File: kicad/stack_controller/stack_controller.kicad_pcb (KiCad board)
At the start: 2 copper layers, 24 parts

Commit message: Possibly final design of stack controller
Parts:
- added U26: ~, Package_DIP:DIP-20_W7.62mm, F.Cu at (40.2, 146.0)
- added U27: ~, Package_DIP:DIP-14_W7.62mm, F.Cu at (40.2, 126.6)
- added U28: ~, Package_DIP:DIP-14_W7.62mm, F.Cu at (51.1, 126.6)
- added U29: ~, Package_DIP:DIP-20_W7.62mm, F.Cu at (51.1, 146.0)
- added U30: ~, Package_DIP:DIP-20_W7.62mm, F.Cu at (62.0, 146.0)
- added U31: ~, Package_DIP:DIP-14_W7.62mm, F.Cu at (62.0, 126.6)
- added U32: ~, Connector_PinHeader_2.54mm:PinHeader_1x08_P2.54mm_Vertical, F.Cu at (73.5, 146.2)
- added U33: ~, Connector_PinHeader_2.54mm:PinHeader_1x16_P2.54mm_Vertical, F.Cu at (36.3, 126.8)
- U12, U8: footprint Package_DIP:DIP-48_W15.24mm -> Package_DIP:DIP-20_W7.62mm
- U9: footprint Package_DIP:DIP-14_W7.62mm -> Package_DIP:DIP-20_W7.62mm
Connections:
- U1 pad 16: Net-(U1-V+) -> Net-(U1-B0)
- U1 pad 7: Net-(U1-B0) -> Net-(U1-C_IN)
- U1 pad 8: Net-(U1-B0) -> Net-(U1-C_IN)
- U10 pad 14: Net-(U1-B0) -> Net-(U1-C_IN)
- U10 pad 28: Net-(U1-V+) -> Net-(U1-B0)
- U11 pad 14: Net-(U1-B0) -> Net-(U1-C_IN)
- U11 pad 22: Net-(U11-OE#) -> Net-(U10-OE#)
- U11 pad 27: Net-(U11-WE#) -> Net-(U10-WE#)
- U11 pad 28: Net-(U1-V+) -> Net-(U1-B0)
- U12 pad 1: Net-(U1-B0) -> Net-(U1-C_IN)
- U12 pad 10: (no net) -> Net-(U1-C_IN)
- U12 pad 11: unconnected-(U12-QA6-Pad11) -> Net-(U12-CLK)
- U12 pad 12: unconnected-(U12-QA7-Pad12) -> Net-(U12-Q7)
- U12 pad 13: Net-(U12-DA0) -> Net-(U12-Q6)
- U12 pad 14: Net-(U1-B1) -> Net-(U12-Q5)
- U12 pad 15: (no net) -> Net-(U12-Q4)
- U12 pad 16: Net-(U12-DA1) -> Net-(U12-Q3)
- U12 pad 17: Net-(U12-QB3) -> Net-(U12-Q2)
- U12 pad 18: (no net) -> Net-(U12-Q1)
- U12 pad 19: Net-(U12-DA2) -> Net-(U12-Q0)
- U12 pad 2: Net-(U12-DB1) -> Net-(U12-D0)
- U12 pad 20: Net-(U12-DA3) -> Net-(U1-B0)
- U12 pad 3: Net-(U12-DB3) -> Net-(U12-D1)
- U12 pad 4: Net-(U1-B0) -> Net-(U12-D2)
- U12 pad 5: Net-(U12-DB5) -> Net-(U12-D3)
- U12 pad 6: Net-(U12-DB6) -> Net-(U12-D4)
- U12 pad 7: Net-(U1-V+) -> Net-(U12-D5)
- U12 pad 8: unconnected-(U12-QA4-Pad8) -> Net-(U12-D6)
- U12 pad 9: unconnected-(U12-QA5-Pad9) -> Net-(U12-D7)
- U13 pad 1: Net-(U12-QB6) -> Net-(U11-CE#)
- U13 pad 10: unconnected-(U13-4A-Pad10) -> Net-(U13-O4)
- U13 pad 11: unconnected-(U13-3Q-Pad11) -> Net-(U13-I4)
- U13 pad 13: unconnected-(U13-3A-Pad13) -> Net-(U1-C_IN)
- U13 pad 14: Net-(U1-V+) -> Net-(U1-B0)
- U13 pad 2: Net-(U12-CLK_B) -> Net-(U10-CE#)
- U13 pad 3: unconnected-(U13-1Q-Pad3) -> Net-(U13-I1)
- U13 pad 4: Net-(U12-QB3) -> Net-(U10-OE#)
- U13 pad 5: Net-(U12-CLK_A) -> Net-(U13-I2)
- U13 pad 6: Net-(U13-2Q) -> Net-(U10-WE#)
- U13 pad 7: Net-(U1-B0) -> Net-(U1-C_IN)
- U13 pad 8: unconnected-(U13-4Q-Pad8) -> Net-(U13-03)
- U13 pad 9: unconnected-(U13-4B-Pad9) -> Net-(U13-I3)
- U14 pad 16: Net-(U1-V+) -> Net-(U1-B0)
- U14 pad 7: Net-(U1-V+) -> Net-(U1-C_IN)
- U14 pad 8: Net-(U1-B0) -> Net-(U1-C_IN)
- U15 pad 16: Net-(U1-V+) -> Net-(U1-B0)
- U15 pad 8: Net-(U1-B0) -> Net-(U1-C_IN)
- U16 pad 11: Net-(U1-V+) -> Net-(U1-B0)
- U16 pad 12: Net-(U16-A3) -> Net-(U12-D3)
- U16 pad 14: Net-(U16-A2) -> Net-(U12-D2)
- U16 pad 15: Net-(U1-V+) -> Net-(U1-B0)
- U16 pad 16: Net-(U1-V+) -> Net-(U1-B0)
- U16 pad 2: Net-(U1-V+) -> Net-(U1-B0)
- U16 pad 3: Net-(U16-A1) -> Net-(U12-D1)
- U16 pad 5: Net-(U16-A0) -> Net-(U12-D0)
- U16 pad 6: Net-(U1-V+) -> Net-(U1-B0)
- U16 pad 8: Net-(U1-B0) -> Net-(U1-C_IN)
- U17 pad 11: Net-(U1-V+) -> Net-(U1-B0)
- U17 pad 12: Net-(U17-A3) -> Net-(U12-D7)
- U17 pad 14: Net-(U17-A2) -> Net-(U12-D6)
- U17 pad 15: Net-(U1-V+) -> Net-(U1-B0)
- U17 pad 16: Net-(U1-V+) -> Net-(U1-B0)
- U17 pad 2: Net-(U1-V+) -> Net-(U1-B0)
- U17 pad 3: Net-(U17-A1) -> Net-(U12-D5)
- U17 pad 5: Net-(U17-A0) -> Net-(U12-D4)
- U17 pad 6: Net-(U1-V+) -> Net-(U1-B0)
- U17 pad 8: Net-(U1-B0) -> Net-(U1-C_IN)
- U18 pad 1: Net-(U1-V+) -> Net-(U1-B0)
- U18 pad 10: Net-(U1-B0) -> Net-(U1-C_IN)
- U18 pad 12: Net-(U15-B0) -> Net-(U15-B3)
- U18 pad 13: Net-(U10-D4) -> Net-(U15-B2)
- U18 pad 14: Net-(U10-D5) -> Net-(U15-B1)
- U18 pad 15: Net-(U15-B1) -> Net-(U15-B0)
- U18 pad 16: Net-(U15-B2) -> Net-(U14-B3)
- U18 pad 17: Net-(U10-D6) -> Net-(U14-B2)
- U18 pad 18: Net-(U10-D7) -> Net-(U14-B1)
- U18 pad 19: Net-(U15-B3) -> Net-(U14-B0)
- U18 pad 2: Net-(U14-B0) -> Net-(U18-D0)
- U18 pad 20: Net-(U1-V+) -> Net-(U1-B0)
- U18 pad 3: Net-(U10-D0) -> Net-(U18-D1)
- U18 pad 4: Net-(U10-D1) -> Net-(U18-D2)
- U18 pad 5: Net-(U14-B1) -> Net-(U18-D3)
- U18 pad 6: Net-(U14-B2) -> Net-(U18-D4)
- U18 pad 7: Net-(U10-D2) -> Net-(U18-D5)
- U18 pad 8: Net-(U10-D3) -> Net-(U18-D6)
- U18 pad 9: Net-(U14-B3) -> Net-(U18-D7)
- U19 pad 1: unconnected-(U19-I0-Pad1) -> Net-(U13-03)
- U19 pad 10: Net-(U10-OE#) -> Net-(U19-4A)
- U19 pad 11: unconnected-(U19-I4-Pad11) -> Net-(U13-I4)
- U19 pad 12: Net-(U10-WE#) -> Net-(U19-2B)
- U19 pad 13: Net-(U19-I5) -> Net-(U13-03)
- U19 pad 14: Net-(U1-V+) -> Net-(U1-B0)
- U19 pad 2: Net-(U11-CE#) -> Net-(U19-1B)
- U19 pad 3: unconnected-(U19-I1-Pad3) -> Net-(U13-I1)
- U19 pad 4: Net-(U11-OE#) -> Net-(U19-1B)
- U19 pad 5: Net-(U19-I2) -> Net-(U19-2B)
- U19 pad 6: Net-(U11-WE#) -> Net-(U13-I3)
- U19 pad 7: Net-(U1-B0) -> Net-(U1-C_IN)
- U19 pad 8: Net-(U10-CE#) -> Net-(U19-4Q)
- U19 pad 9: unconnected-(U19-I3-Pad9) -> Net-(U12-CLK)
- U2 pad 16: Net-(U1-V+) -> Net-(U1-B0)
- U2 pad 8: Net-(U1-B0) -> Net-(U1-C_IN)
- U20 pad 10: Net-(U14-Σ3) -> Net-(U14-Σ2)
- U20 pad 11: Net-(U14-A3) -> Net-(U14-A2)
- U20 pad 12: Net-(U10-A2) -> Net-(U10-A3)
- U20 pad 13: Net-(U14-Σ2) -> Net-(U14-Σ3)
- U20 pad 14: Net-(U14-A2) -> Net-(U14-A3)
- U20 pad 15: Net-(U1-B0) -> Net-(U1-C_IN)
- U20 pad 16: Net-(U1-V+) -> Net-(U1-B0)
- U20 pad 8: Net-(U1-B0) -> Net-(U1-C_IN)
- U20 pad 9: Net-(U10-A3) -> Net-(U10-A2)
- U21 pad 10: Net-(U15-Σ3) -> Net-(U15-Σ2)
- U21 pad 11: Net-(U15-A3) -> Net-(U15-A2)
- U21 pad 12: Net-(U10-A6) -> Net-(U10-A7)
- U21 pad 13: Net-(U15-Σ2) -> Net-(U15-Σ3)
- U21 pad 14: Net-(U15-A2) -> Net-(U15-A3)
- U21 pad 15: Net-(U1-B0) -> Net-(U1-C_IN)
- U21 pad 16: Net-(U1-V+) -> Net-(U1-B0)
- U21 pad 8: Net-(U1-B0) -> Net-(U1-C_IN)
- U21 pad 9: Net-(U10-A7) -> Net-(U10-A6)
- U22 pad 10: Net-(U16-Σ3) -> Net-(U16-Σ2)
- U22 pad 11: Net-(U16-A3) -> Net-(U12-D2)
- U22 pad 12: Net-(U10-A10) -> Net-(U10-A11)
- U22 pad 13: Net-(U16-Σ2) -> Net-(U16-Σ3)
- U22 pad 14: Net-(U16-A2) -> Net-(U12-D3)
- U22 pad 15: Net-(U1-B0) -> Net-(U1-C_IN)
- U22 pad 16: Net-(U1-V+) -> Net-(U1-B0)
- U22 pad 2: Net-(U16-A0) -> Net-(U12-D0)
- U22 pad 5: Net-(U16-A1) -> Net-(U12-D1)
- U22 pad 8: Net-(U1-B0) -> Net-(U1-C_IN)
- U22 pad 9: Net-(U10-A11) -> Net-(U10-A10)
- U23 pad 10: Net-(U17-Σ3) -> Net-(U17-Σ2)
- U23 pad 11: Net-(U17-A3) -> Net-(U12-D6)
- U23 pad 12: Net-(U10-A14) -> Net-(U11-CE#)
- U23 pad 13: Net-(U17-Σ2) -> Net-(U17-Σ3)
- U23 pad 14: Net-(U17-A2) -> Net-(U12-D7)
- U23 pad 15: Net-(U1-B0) -> Net-(U1-C_IN)
- U23 pad 16: Net-(U1-V+) -> Net-(U1-B0)
- U23 pad 2: Net-(U17-A0) -> Net-(U12-D4)
- U23 pad 5: Net-(U17-A1) -> Net-(U12-D5)
- U23 pad 8: Net-(U1-B0) -> Net-(U1-C_IN)
- U23 pad 9: Net-(U23-Q3) -> Net-(U10-A14)
- U24 pad 1: Net-(U23-Q3) -> Net-(U24-1A)
- U24 pad 10: unconnected-(U24-Q2-Pad10) -> Net-(U24-4A)
- U24 pad 11: unconnected-(U24-Q3-Pad11) -> Net-(U24-3Q)
- U24 pad 12: unconnected-(U24-3A-Pad12) -> Net-(U24-2A)
- U24 pad 13: unconnected-(U24-3B-Pad13) -> Net-(U24-3A)
- U24 pad 14: Net-(U1-V+) -> Net-(U1-B0)
- U24 pad 2: unconnected-(U24-0B-Pad2) -> Net-(U1-B1)
- U24 pad 3: Net-(U19-I2) -> Net-(U24-1Q)
- U24 pad 4: Net-(U19-I5) -> Net-(U24-2A)
- U24 pad 5: Net-(U24-1A) -> Net-(U24-2B)
- U24 pad 6: unconnected-(U24-1B-Pad6) -> Net-(U13-I2)
- U24 pad 7: Net-(U1-B0) -> Net-(U1-C_IN)
- U24 pad 8: unconnected-(U24-2A-Pad8) -> Net-(U24-4Q)
- U24 pad 9: unconnected-(U24-2B-Pad9) -> Net-(U24-2A)
- U25 pad 1: Net-(U23-Q3) -> Net-(U25-0A)
- U25 pad 10: unconnected-(U25-O4-Pad10) -> Net-(U24-3A)
- U25 pad 11: unconnected-(U25-I4-Pad11) -> Net-(U25-Q3)
- U25 pad 12: unconnected-(U25-O5-Pad12) -> Net-(U13-I3)
- U25 pad 13: unconnected-(U25-I5-Pad13) -> Net-(U19-4Q)
- U25 pad 14: Net-(U1-V+) -> Net-(U1-B0)
- U25 pad 2: Net-(U24-1A) -> Net-(U1-B1)
- U25 pad 3: unconnected-(U25-I1-Pad3) -> Net-(U19-1B)
- U25 pad 5: unconnected-(U25-I2-Pad5) -> Net-(U1-C_IN)
- U25 pad 6: unconnected-(U25-O2-Pad6) -> Net-(U1-C_IN)
- U25 pad 7: Net-(U1-B0) -> Net-(U1-C_IN)
- U25 pad 8: unconnected-(U25-03-Pad8) -> Net-(U25-2A)
- U25 pad 9: unconnected-(U25-I3-Pad9) -> Net-(U25-2B)
- U3 pad 12: Net-(U3-A3) -> Net-(U12-Q3)
- U3 pad 14: Net-(U3-A2) -> Net-(U12-Q2)
- U3 pad 16: Net-(U1-V+) -> Net-(U1-B0)
- U3 pad 3: Net-(U3-A1) -> Net-(U12-Q1)
- U3 pad 5: Net-(U3-A0) -> Net-(U12-Q0)
- U3 pad 8: Net-(U1-B0) -> Net-(U1-C_IN)
- U4 pad 12: Net-(U4-A3) -> Net-(U12-Q7)
- U4 pad 14: Net-(U4-A2) -> Net-(U12-Q6)
- U4 pad 16: Net-(U1-V+) -> Net-(U1-B0)
- U4 pad 3: Net-(U4-A1) -> Net-(U12-Q5)
- U4 pad 5: Net-(U4-A0) -> Net-(U12-Q4)
- U4 pad 8: Net-(U1-B0) -> Net-(U1-C_IN)
- U6 pad 1: Net-(U1-V+) -> Net-(U1-C_IN)
- U6 pad 10: Net-(U1-B0) -> Net-(U1-C_IN)
- U6 pad 11: Net-(U13-2Q) -> Net-(U19-4A)
- U6 pad 12: Net-(U15-A0) -> Net-(U15-A3)
- U6 pad 13: Net-(U2-Σ0) -> Net-(U15-A2)
- U6 pad 14: Net-(U2-Σ1) -> Net-(U15-A1)
- U6 pad 15: Net-(U15-A1) -> Net-(U15-A0)
- U6 pad 16: Net-(U15-A2) -> Net-(U14-A3)
- U6 pad 17: Net-(U2-Σ2) -> Net-(U14-A2)
- U6 pad 18: Net-(U2-Σ3) -> Net-(U14-A1)
- U6 pad 19: Net-(U15-A3) -> Net-(U14-A0)
- U6 pad 2: Net-(U14-A0) -> Net-(U1-Σ0)
- U6 pad 20: Net-(U1-V+) -> Net-(U1-B0)
- U6 pad 3: Net-(U1-Σ0) -> Net-(U1-Σ1)
- U6 pad 4: Net-(U1-Σ1) -> Net-(U1-Σ2)
- U6 pad 5: Net-(U14-A1) -> Net-(U1-Σ3)
- U6 pad 6: Net-(U14-A2) -> Net-(U2-Σ0)
- U6 pad 7: Net-(U1-Σ2) -> Net-(U2-Σ1)
- U6 pad 8: Net-(U1-Σ3) -> Net-(U2-Σ2)
- U6 pad 9: Net-(U14-A3) -> Net-(U2-Σ3)
- U7 pad 1: Net-(U1-V+) -> Net-(U1-C_IN)
- U7 pad 10: Net-(U1-B0) -> Net-(U1-C_IN)
- U7 pad 11: Net-(U13-2Q) -> Net-(U19-4A)
- U7 pad 12: Net-(U17-A0) -> Net-(U12-D7)
- U7 pad 13: Net-(U4-Σ0) -> Net-(U12-D6)
- U7 pad 14: Net-(U4-Σ1) -> Net-(U12-D5)
- U7 pad 15: Net-(U17-A1) -> Net-(U12-D4)
- U7 pad 16: Net-(U17-A2) -> Net-(U12-D3)
- U7 pad 17: Net-(U4-Σ2) -> Net-(U12-D2)
- U7 pad 18: Net-(U4-Σ3) -> Net-(U12-D1)
- U7 pad 19: Net-(U17-A3) -> Net-(U12-D0)
- U7 pad 2: Net-(U16-A0) -> Net-(U3-Σ0)
- U7 pad 20: Net-(U1-V+) -> Net-(U1-B0)
- U7 pad 3: Net-(U3-Σ0) -> Net-(U3-Σ1)
- U7 pad 4: Net-(U3-Σ1) -> Net-(U3-Σ2)
- U7 pad 5: Net-(U16-A1) -> Net-(U3-Σ3)
- U7 pad 6: Net-(U16-A2) -> Net-(U4-Σ0)
- U7 pad 7: Net-(U3-Σ2) -> Net-(U4-Σ1)
- U7 pad 8: Net-(U3-Σ3) -> Net-(U4-Σ2)
- U7 pad 9: Net-(U16-A3) -> Net-(U4-Σ3)
- U8 pad 1: Net-(U1-B0) -> Net-(U1-C_IN)
- U8 pad 10: (no net) -> Net-(U1-C_IN)
- U8 pad 11: Net-(U2-A2) -> Net-(U12-CLK)
- U8 pad 13: Net-(U3-A0) -> Net-(U2-A2)
- U8 pad 14: Net-(U3-A1) -> Net-(U2-A1)
- U8 pad 15: (no net) -> Net-(U2-A0)
- U8 pad 16: Net-(U3-A2) -> Net-(U1-A3)
- U8 pad 17: Net-(U3-A3) -> Net-(U1-A2)
- U8 pad 18: (no net) -> Net-(U1-A1)
- U8 pad 19: Net-(U4-A0) -> Net-(U1-A0)
- U8 pad 2: Net-(U1-A0) -> Net-(U14-A0)
- U8 pad 20: Net-(U4-A1) -> Net-(U1-B0)
- U8 pad 3: Net-(U1-A1) -> Net-(U14-A1)
- U8 pad 4: Net-(U1-B0) -> Net-(U14-A2)
- U8 pad 5: Net-(U1-A2) -> Net-(U14-A3)
- U8 pad 6: Net-(U1-A3) -> Net-(U15-A0)
- U8 pad 7: Net-(U1-V+) -> Net-(U15-A1)
- U8 pad 8: Net-(U2-A0) -> Net-(U15-A2)
- U8 pad 9: Net-(U2-A1) -> Net-(U15-A3)
- U9 pad 1: Net-(U12-DB0) -> Net-(U1-C_IN)
- U9 pad 10: unconnected-(U9-Q2-Pad10) -> Net-(U1-C_IN)
- U9 pad 11: unconnected-(U9-Q3-Pad11) -> Net-(U24-2A)
- U9 pad 12: unconnected-(U9-3A-Pad12) -> Net-(U26-D6)
- U9 pad 13: unconnected-(U9-3B-Pad13) -> Net-(U26-D5)
- U9 pad 14: Net-(U1-V+) -> Net-(U24-4A)
- U9 pad 2: Net-(U5-READ_0) -> Net-(U26-Q0)
- U9 pad 3: Net-(U12-DB2) -> Net-(U24-3A)
- U9 pad 4: Net-(U12-DB4) -> Net-(U26-Q2)
- U9 pad 5: Net-(U5-READ_0) -> Net-(U19-2B)
- U9 pad 6: Net-(U5-READ_1) -> Net-(U25-2B)
- U9 pad 7: Net-(U1-B0) -> Net-(U26-Q4)
- U9 pad 8: unconnected-(U9-2A-Pad8) -> Net-(U25-2A)
- U9 pad 9: unconnected-(U9-2B-Pad9) -> Net-(U26-Q5)

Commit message: kicad stuff and timing
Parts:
- added U34: ~, custom_footprint_library:jumper, F.Cu at (256.5, 212.9)
- added U35: ~, custom_footprint_library:jumper, F.Cu at (256.5, 220.5)
- added U36: ~, custom_footprint_library:jumper, F.Cu at (256.4, 228.3)
- added U37: ~, custom_footprint_library:jumper, F.Cu at (256.5, 236.3)
- added U38: ~, custom_footprint_library:jumper, F.Cu at (256.5, 244.3)
- added U39: ~, custom_footprint_library:jumper, F.Cu at (300.7, 213.3)
- added U40: ~, custom_footprint_library:jumper, F.Cu at (300.7, 221.3)
- added U41: ~, custom_footprint_library:jumper, F.Cu at (300.7, 229.2)
- added U42: ~, custom_footprint_library:jumper, F.Cu at (300.7, 236.8)
- added U43: ~, custom_footprint_library:jumper, F.Cu at (300.7, 244.6)
- added U44: ~, custom_footprint_library:jumper, F.Cu at (300.6, 252.5)
- added U45: ~, custom_footprint_library:jumper, F.Cu at (256.8, 257.3)
- added U46: ~, custom_footprint_library:jumper, F.Cu at (256.8, 265.3)
- added U5: ~, Connector_PinHeader_2.54mm:PinHeader_1x22_P2.54mm_Vertical, F.Cu at (151.5, 259.5)
- moved U29 284.4 mm to (331.9, 190.9), turned to -90 degrees
- moved U33 269.8 mm to (305.5, 143.7), turned to 90 degrees
- moved U13 263.9 mm to (342.0, 210.3)
- moved U32 258.9 mm to (329.3, 185.9), turned to -90 degrees
- moved U19 239.0 mm to (342.4, 179.9)
- moved U30 219.7 mm to (276.3, 194.1), turned to 90 degrees
- moved U27 213.4 mm to (216.0, 247.5), turned to -90 degrees
- moved U26 209.4 mm to (225.9, 242.8)
- moved U1 203.8 mm to (229.7, 119.1)
- moved U11 196.6 mm to (323.7, 154.8), turned to -90 degrees
- moved U31 192.0 mm to (232.7, 214.4)
- moved U16 191.7 mm to (243.1, 181.5), turned to -90 degrees
- moved U28 185.4 mm to (216.2, 210.9)
- moved U10 184.7 mm to (361.1, 154.8), turned to -90 degrees
- moved U9 181.4 mm to (185.0, 239.8)
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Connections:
- U13 pad 12: unconnected-(U13-O5-Pad12) -> Net-(U13-O5)
- U13 pad 13: Net-(U1-C_IN) -> Net-(U13-I5)
- U18 pad 1: Net-(U1-B0) -> Net-(U1-C_IN)
- U24 pad 2: Net-(U1-B1) -> Net-(U24-1B)
- U24 pad 6: Net-(U13-I2) -> Net-(U24-2Q)
- U25 pad 12: Net-(U13-I3) -> Net-(U25-3A)
- U25 pad 13: Net-(U19-4Q) -> Net-(U25-3B)
- U25 pad 2: Net-(U1-B1) -> Net-(U24-1B)
- U25 pad 3: Net-(U19-1B) -> Net-(U25-Q0)
- U26 pad 16: Net-(U19-2B) -> Net-(U26-Q3)
- U27 pad 10: Net-(U19-4A) -> Net-(U27-Q2)
- U27 pad 11: Net-(U12-CLK) -> Net-(U27-Q3)
- U27 pad 4: Net-(U20-S) -> Net-(U27-Q1)
- U28 pad 1: Net-(U19-1B) -> Net-(U25-Q0)
- U28 pad 6: Net-(U18-CLK) -> Net-(U28-2Q)
- U29 pad 1: Net-(U26-Q0) -> Net-(U13-O5)
- U29 pad 11: Net-(U27-3B) -> Net-(U29-CLK)
- U30 pad 11: Net-(U24-3Q) -> Net-(U30-CLK)
- U9 pad 5: Net-(U19-2B) -> Net-(U26-Q3)
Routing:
- net Net-(U1-C_IN): track 0.00 -> 1158.8 mm, vias 0 -> 5
- net Net-(U1-B0): track 0.00 -> 828.4 mm, vias 0 -> 8
- net Net-(U15-A0): track 0.00 -> 273.5 mm, vias 0 -> 5
- net Net-(U1-B1): track 0.00 -> 272.3 mm, vias 0 -> 4
- net Net-(U12-CLK): track 0.00 -> 255.5 mm, vias 0 -> 3
- net Net-(U14-A0): track 0.00 -> 251.6 mm, vias 0 -> 2
- net Net-(U15-A1): track 0.00 -> 224.2 mm, vias 0 -> 4
- net Net-(U14-A1): track 0.00 -> 210.6 mm, vias 0 -> 3
- net Net-(U19-4A): track 0.00 -> 206.1 mm, vias 0 -> 1
- net Net-(U18-D0): track 0.00 -> 205.9 mm, vias 0 -> 1
- net Net-(U14-A3): track 0.00 -> 202.8 mm, vias 0 -> 4
- net Net-(U18-D1): track 0.00 -> 200.0 mm
- net Net-(U18-D2): track 0.00 -> 195.7 mm, vias 0 -> 1
- net Net-(U18-D3): track 0.00 -> 190.8 mm, vias 0 -> 1
- net Net-(U14-A2): track 0.00 -> 190.1 mm, vias 0 -> 3
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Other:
- board text added: "MEMORY BUS SIMULTANEOUS WRITE ADDRESS LATCHES SIMULTANEOUS HIGH"
- board text added: "Pointer adder input latch CLK Pointer inc (0) / dec (1) select Pointer latch CLK ToS (0) / offset (1) select Offset latch CLK"
- board text added: "Read (mem output enable) Write Input latch CLK Input latch output enable Output latch CLK Output latch output enable"

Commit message: stuff
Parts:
- added U47: ~, Package_DIP:DIP-14_W7.62mm, F.Cu at (115.0, 151.1)
- U5: footprint Connector_PinHeader_2.54mm:PinHeader_1x22_P2.54mm_Vertical -> Connector_PinHeader_2.54mm:PinHeader_1x23_P2.54mm_Vertical
- moved U1 155.9 mm to (105.5, 24.8)
- moved U10 155.9 mm to (236.9, 60.5)
- moved U11 155.9 mm to (199.5, 60.5)
- moved U13 155.9 mm to (217.8, 116.1)
- moved U14 155.9 mm to (42.8, 72.0)
- moved U15 155.9 mm to (84.5, 78.3)
- moved U16 155.9 mm to (118.9, 87.2)
- moved U17 155.9 mm to (128.5, 80.8)
- moved U19 155.9 mm to (218.2, 85.6)
- moved U2 155.9 mm to (85.5, 25.3)
- moved U20 155.9 mm to (136.9, 67.5)
- moved U21 155.9 mm to (148.4, 50.5)
- moved U22 155.9 mm to (151.9, 32.6)
- moved U24 155.9 mm to (55.2, 120.2)
- moved U25 155.9 mm to (73.2, 116.1)
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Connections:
- U44 pad 1: Net-(U26-Q0) -> Net-(U44-IN)
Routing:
- net Net-(U47-1B): track 0.00 -> 118.7 mm, vias 0 -> 8
- net Net-(U26-Q0): track 186.0 -> 116.9 mm, vias 2 -> 1
- net Net-(U44-IN): track 0.00 -> 67.2 mm, vias 0 -> 1
- net Net-(U26-Q5): track 0.00 -> 62.2 mm
- net Net-(U1-C_IN): track 1158.8 -> 1210.7 mm
- net Net-(U26-Q3): track 140.7 -> 166.9 mm, vias 1 -> 2
- net Net-(U25-3A): track 98.5 -> 113.8 mm, vias 1 -> 3
- net Net-(U26-CLK): track 151.3 -> 139.0 mm, vias 2 -> 1
- net Net-(U25-0A): track 93.7 -> 82.1 mm
- net Net-(U18-D7): track 174.3 -> 162.8 mm
- net Net-(U25-2B): track 80.0 -> 68.5 mm, vias 3 -> 2
- net Net-(U25-Q3): track 60.0 -> 48.5 mm
- net Net-(U18-D5): track 181.2 -> 170.0 mm
- net Net-(U24-2A): track 125.0 -> 114.6 mm, vias 0 -> 1
- net Net-(U18-D3): track 190.8 -> 180.7 mm, vias 1 -> 0
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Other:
- board outline added: 208.5 x 156.5 mm

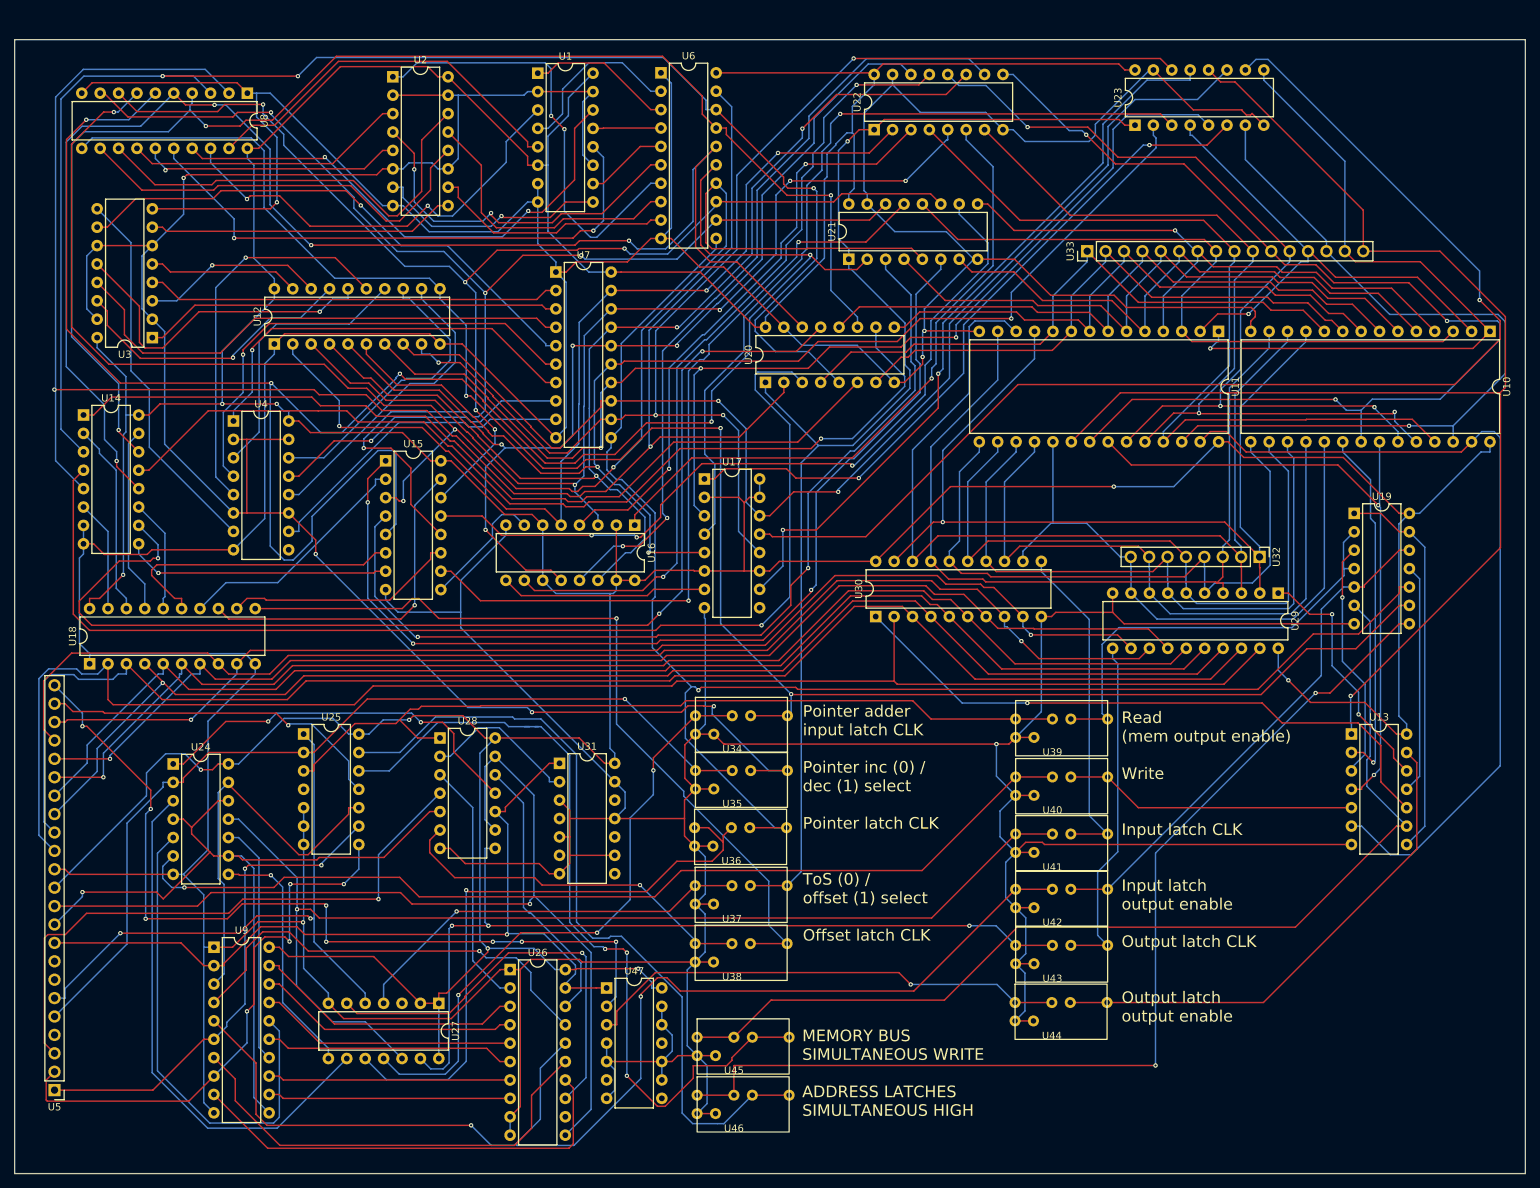
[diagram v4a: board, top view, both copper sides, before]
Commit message: Increased clock PCB clearances
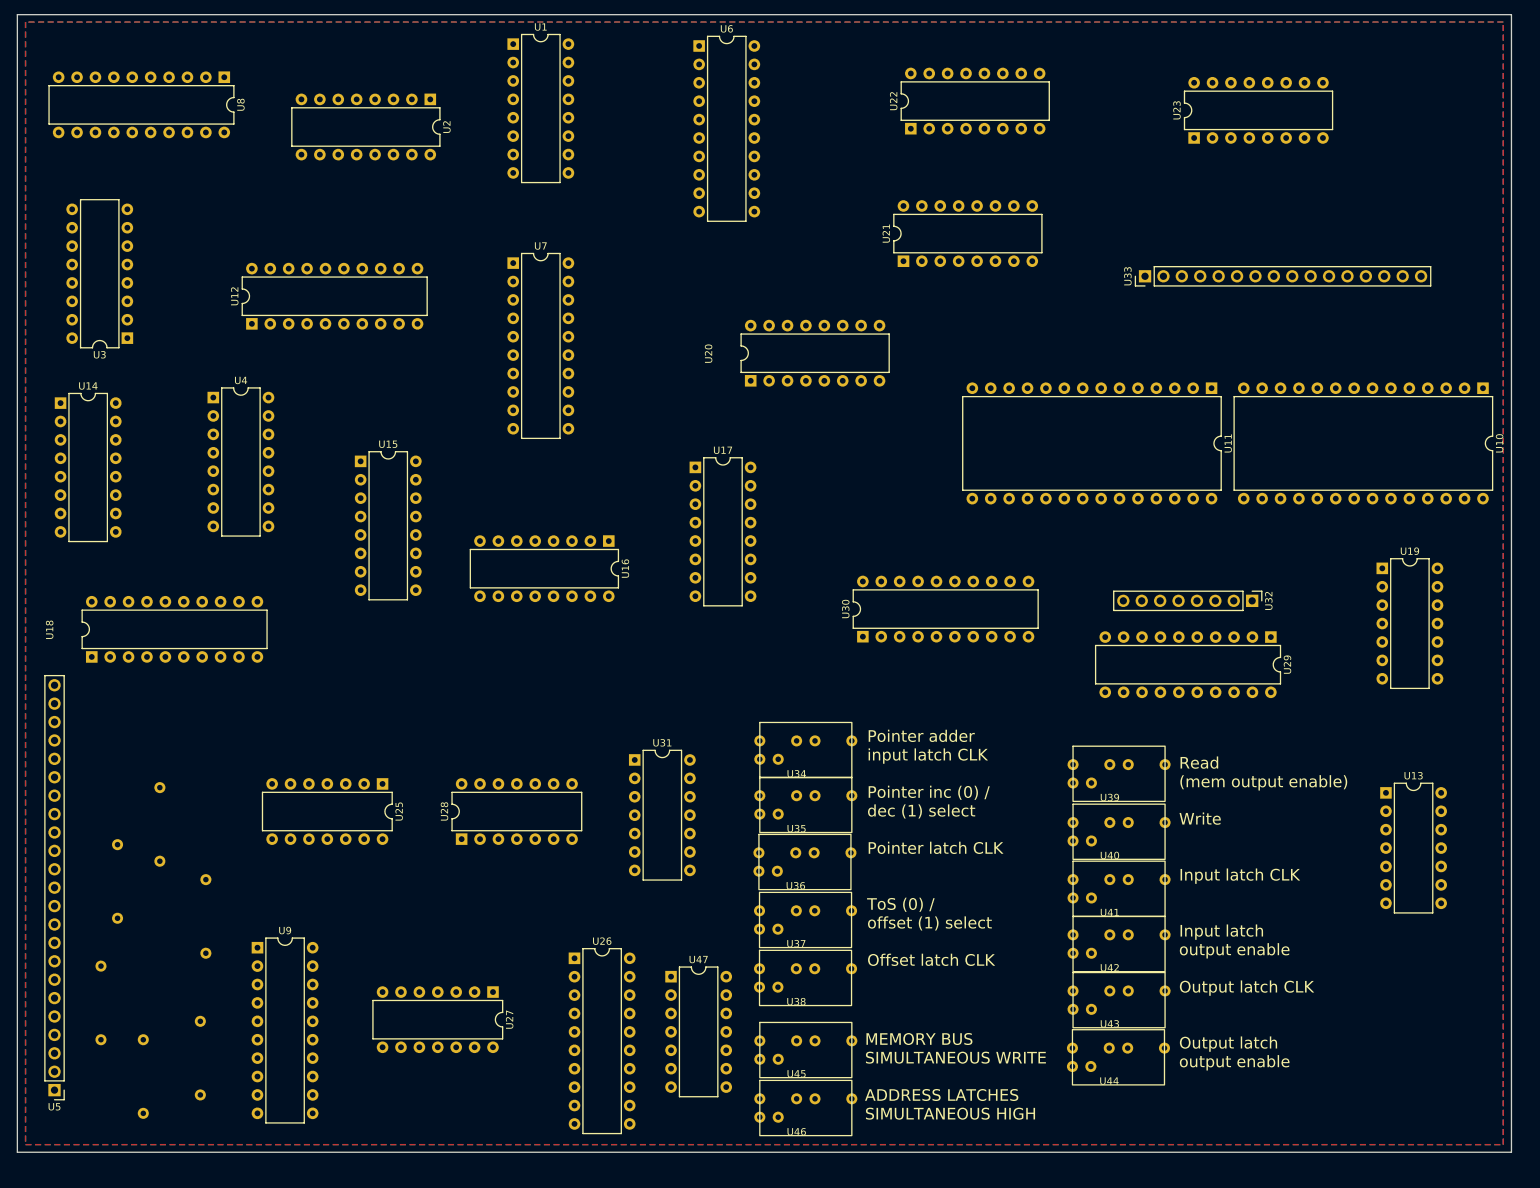
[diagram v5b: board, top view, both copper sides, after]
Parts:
- removed U24: ~, Package_DIP:DIP-14_W7.62mm
- added R1: 1k, custom_footprint_library:0.4_pitch_resistor, B.Cu at (45.2, 153.2)
- added R2: 1k, custom_footprint_library:0.4_pitch_resistor, B.Cu at (51.1, 163.3)
- added R3: 1k, custom_footprint_library:0.4_pitch_resistor, B.Cu at (59.7, 141.2)
- added R4: 1k, custom_footprint_library:0.4_pitch_resistor, B.Cu at (47.5, 136.4)
- added R5: 1k, custom_footprint_library:0.4_pitch_resistor, B.Cu at (58.9, 160.8)
- added R6: 1k, custom_footprint_library:0.4_pitch_resistor, B.Cu at (53.3, 128.5)
- moved U28 14.3 mm to (95.0, 130.6), turned to 90 degrees
- moved U25 12.9 mm to (84.1, 122.9), turned to -90 degrees
- moved U31 10.4 mm to (118.9, 119.6)
- moved U44 10.1 mm to (184.4, 164.5)
- moved U42 10.1 mm to (184.5, 148.8)
- moved U40 10.1 mm to (184.5, 133.3)
- moved U39 10.1 mm to (184.5, 125.3)
- moved U41 10.1 mm to (184.5, 141.2)
- moved U43 10.1 mm to (184.5, 156.6)
- moved U36 9.54 mm to (141.1, 137.5)
- moved U35 9.54 mm to (141.2, 129.6)
- moved U37 9.54 mm to (141.2, 145.5)
- moved U38 9.54 mm to (141.2, 153.5)
- moved U34 9.54 mm to (141.2, 122.1)
- moved U13 9.41 mm to (222.6, 124.2)
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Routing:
- net Net-(U1-C_IN): track 1210.7 -> 0.00 mm, vias 5 -> 0
- net Net-(U1-B0): track 833.7 -> 0.00 mm, vias 9 -> 0
- net Net-(U1-B1): track 277.4 -> 0.00 mm, vias 4 -> 0
- net Net-(U15-A0): track 273.5 -> 0.00 mm, vias 5 -> 0
- net Net-(U12-CLK): track 260.6 -> 0.00 mm, vias 3 -> 0
- net Net-(U14-A0): track 251.6 -> 0.00 mm, vias 2 -> 0
- net Net-(U15-A1): track 224.2 -> 0.00 mm, vias 4 -> 0
- net Net-(U18-D0): track 212.3 -> 0.00 mm
- net Net-(U19-4A): track 211.2 -> 0.00 mm, vias 1 -> 0
- net Net-(U14-A1): track 210.6 -> 0.00 mm, vias 3 -> 0
- net Net-(U14-A3): track 202.8 -> 0.00 mm, vias 4 -> 0
- net Net-(U18-D1): track 202.4 -> 0.00 mm
- net Net-(U14-A2): track 190.1 -> 0.00 mm, vias 3 -> 0
- net Net-(U11-CE#): track 187.0 -> 0.00 mm, vias 1 -> 0
- net Net-(U18-D2): track 186.0 -> 0.00 mm, vias 1 -> 0
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- added copper zone on F.Cu, net Net-(U1-B0)
- added copper zone on B.Cu, net Net-(U1-C_IN)
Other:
- board size 208.5 x 156.5 mm -> 206.2 x 157 mm

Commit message: Working on GPRAM schematic
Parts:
- added U24: ~, Package_DIP:DIP-14_W7.62mm, F.Cu at (99.1, 138.4)
- moved U27 3.28 mm to (99.3, 154.9)
